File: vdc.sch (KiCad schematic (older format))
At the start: 37 parts, among them CN10 RGBI 9-pin DIN, Q1 2SC1815, Q4 2SC1815, Q5 2SC1815, U22 8563, U23 4464, U24 74LS244, U25 4464, U29 7406, U54 74LS32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

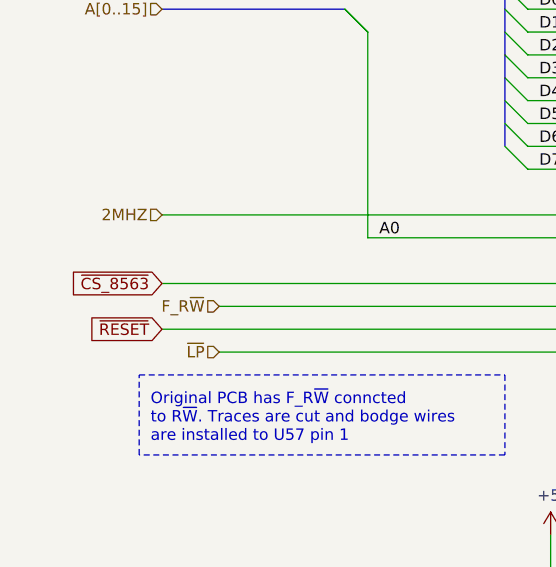
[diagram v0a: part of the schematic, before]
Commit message: Clean up schematic
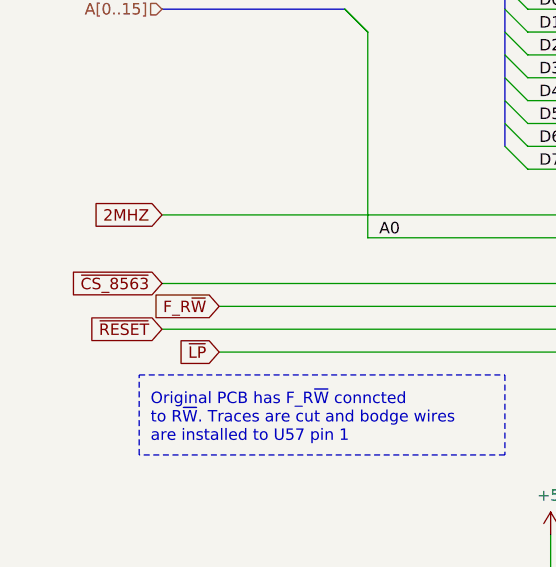
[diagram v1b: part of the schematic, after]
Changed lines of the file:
@@
 Wire Wire Line
 	2850 4200 1000 4200
-Text HLabel 1000 4200 0    50   Input ~ 0
-2MHZ
-Text HLabel 1250 4600 0    50   Input ~ 0
-F_R~W
-Text HLabel 1250 4800 0    50   Input ~ 0
-~LP
 Wire Wire Line
 	1250 4600 2850 4600
@@
 Wire Bus Line
 	8250 1250 8250 2650
+Text GLabel 1250 4600 0    50   Input ~ 0
+F_R~W
+Text GLabel 1250 4800 0    50   Input ~ 0
+~LP
+Text GLabel 1000 4200 0    50   Input ~ 0
+2MHZ
 $EndSCHEMATC
